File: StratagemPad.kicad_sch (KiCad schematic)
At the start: 0 parts

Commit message: assign footprints + update pcb
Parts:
- added SW1: SW_Push, PCM_Switch_Keyboard_Hotswap_Kailh:SW_Hotswap_Kailh_MX_1.50u_90deg, symbol Switch:SW_Push
- added SW2, SW3, SW4, SW5: SW_Push, PCM_Switch_Keyboard_Hotswap_Kailh:SW_Hotswap_Kailh_MX_1.00u, symbol Switch:SW_Push
- added U1: XIAO-ESP32-C6-SMD, Seeed_Studio_XIAO_Series:XIAO-ESP32-S3-DIP, symbol Seeed_Studio_XIAO_Series:XIAO-ESP32-C6-SMD

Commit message: add components + some pcb editing
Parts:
- added D1: LED_BGKR, LED_THT:LED_D5.0mm-4_RGB, symbol Device:LED_BGKR
- added J1: Conn_01x02_Pin, Connector_JST:JST_PH_B2B-PH-K_1x02_P2.00mm_Vertical, symbol Connector:Conn_01x02_Pin
- added R1, R2, R3: R, Resistor_THT:R_Axial_DIN0204_L3.6mm_D1.6mm_P2.54mm_Vertical, symbol Device:R
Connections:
- net at U1.1 (D0): now also R1.2, R2.2
- net Ground: now reaches U1.13 (GND)
- net Ground: now also SW1.1, SW2.1, SW3.1, SW4.1, SW5.1, R3.1
- net LED R: now reaches U1.2 (D1)
- net LED R: now also D1.4 (RA)
- net LED G: now reaches U1.3 (D2)
- net LED G: now also D1.2 (GA)
- net LED B: now reaches U1.4 (D3)
- net LED B: now also D1.1 (BA)
- net Button 1: now reaches U1.5 (D4)
- net Button 1: now also SW1.2
- net Button 2: now reaches U1.6 (D5)
- net Button 2: now also SW2.2
- net Button 3: now reaches U1.7 (D6)
- net Button 3: now also SW3.2
- net Button 4: now reaches U1.8 (D7)
- net Button 4: now also SW4.2
- net Button 5: now reaches U1.9 (D8)
- net Button 5: now also SW5.2
- new net: J1.1 (Pin_1), R1.1
- new net: J1.2 (Pin_2), R2.1
- new net: D1.3 (K), R3.2

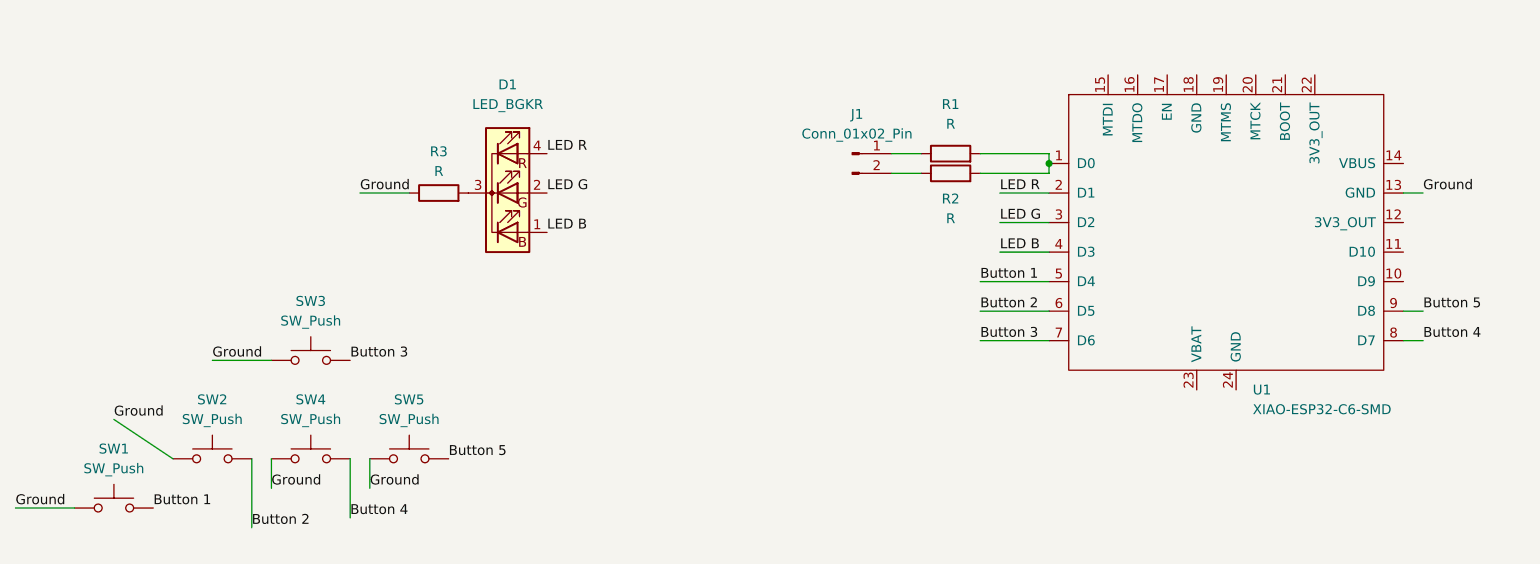
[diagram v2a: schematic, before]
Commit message: use global labels + update pcb
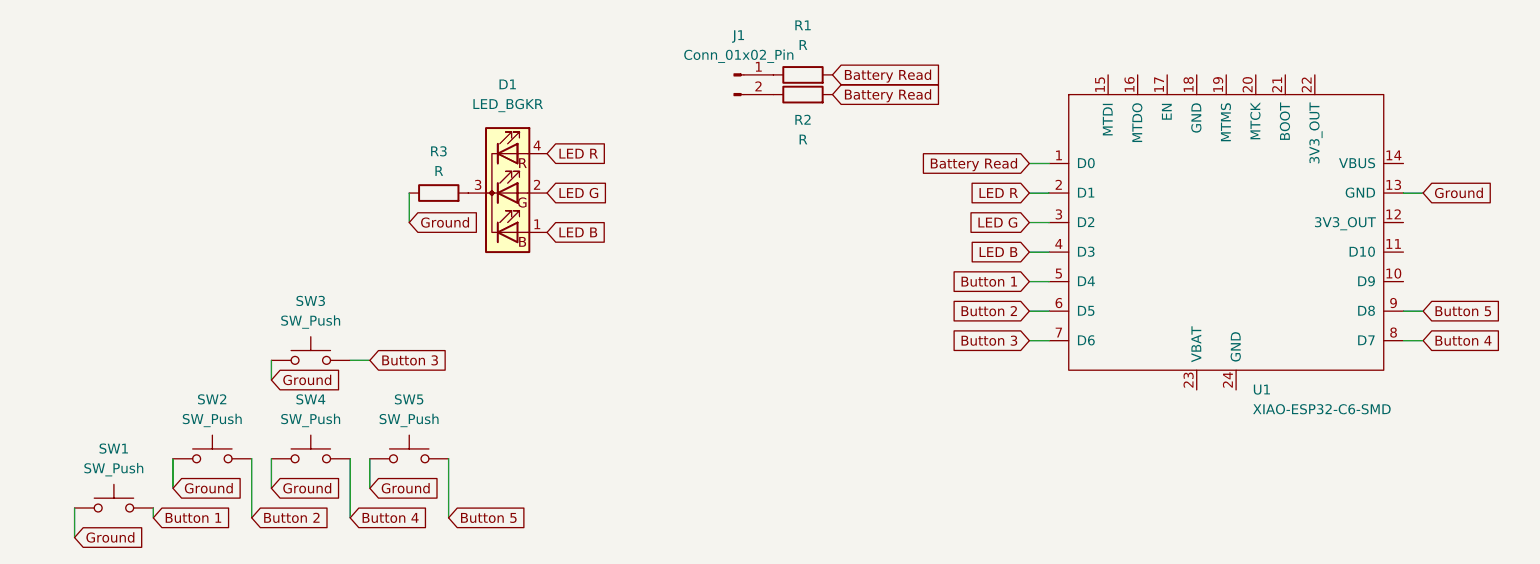
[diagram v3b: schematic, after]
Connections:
- net Battery Read: now reaches R1.2, R2.2, U1.1 (D0)
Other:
- moved on the sheet: J1, R1, R2

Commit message: set pcb origin point + move with reference
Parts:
- D1: footprint LED_THT:LED_D5.0mm-4_RGB -> LED_THT:LED_D5.0mm-4_RGB_Wide_Pins
- U1: footprint Seeed_Studio_XIAO_Series:XIAO-ESP32-S3-DIP -> Seeed_Studio_XIAO_Series:XIAO-ESP32-C6-DIP
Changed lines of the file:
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@@
 			)
 		)
-		(property "Footprint" "Seeed_Studio_XIAO_Series:XIAO-ESP32-S3-DIP"
+		(property "Footprint" "Seeed_Studio_XIAO_Series:XIAO-ESP32-C6-DIP"
 			(at 215.9 48.26 0)
 			(hide yes)
@@
 			)
 		)
-		(property "Footprint" "LED_THT:LED_D5.0mm-4_RGB"
+		(property "Footprint" "LED_THT:LED_D5.0mm-4_RGB_Wide_Pins"
 			(at 133.35 50.8 0)
 			(hide yes)
